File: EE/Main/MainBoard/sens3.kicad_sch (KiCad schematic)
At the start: 3 parts, among them J4 Conn_02x13_Odd_Even

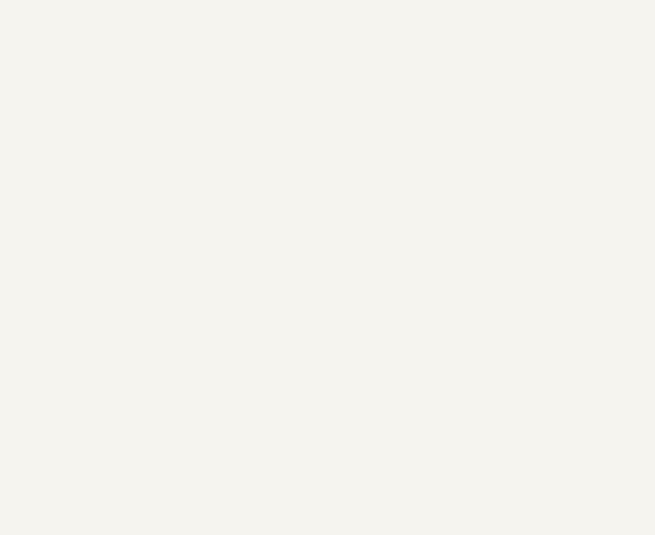
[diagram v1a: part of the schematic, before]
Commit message: WIP - Moving Sensor to IO Expander
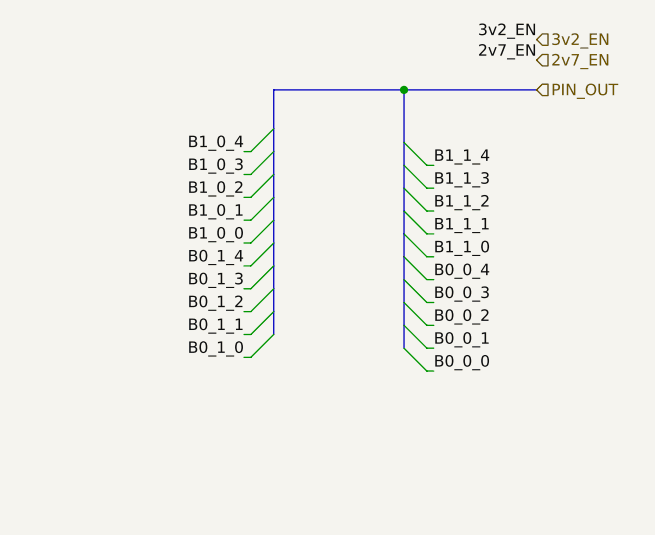
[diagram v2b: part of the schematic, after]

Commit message: Updated layout, and placement for main board
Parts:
- removed J4: Conn_02x13_Odd_Even, Connector_PinHeader_1.27mm:PinHeader_2x13_P1.27mm_Vertical_SMD, symbol Connector_Generic:Conn_02x13_Odd_Even
- added J4: Conn_01x04_Male, Connector_PinSocket_2.54mm:PinSocket_1x04_P2.54mm_Vertical, symbol Connector:Conn_01x04_Male
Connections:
- net GND: now also J4.4 (Pin_4)
- net VCC: now also J4.1 (Pin_1)
- new net SCL: J4.2 (Pin_2)
- new net SDA: J4.3 (Pin_3)
- no-connect marks 2 -> 0

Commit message: Routine Update
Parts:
- H7, H8: footprint MountingHole:MountingHole_2.5mm -> MountingHole:MountingHole_2.7mm
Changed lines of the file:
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@@
       (effects (font (size 1.27 1.27)) (justify left))
     )
-    (property "Footprint" "MountingHole:MountingHole_2.5mm" (id 2) (at 94.488 93.472 0)
+    (property "Footprint" "MountingHole:MountingHole_2.7mm" (id 2) (at 94.488 93.472 0)
       (effects (font (size 1.27 1.27)) hide)
     )
@@
       (effects (font (size 1.27 1.27)) (justify left))
     )
-    (property "Footprint" "MountingHole:MountingHole_2.5mm" (id 2) (at 94.488 49.276 0)
+    (property "Footprint" "MountingHole:MountingHole_2.7mm" (id 2) (at 94.488 49.276 0)
       (effects (font (size 1.27 1.27)) hide)
     )
